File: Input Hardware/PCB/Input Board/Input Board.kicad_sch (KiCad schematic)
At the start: 6 parts

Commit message: end me
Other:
- sheet Demux & Amplifier 1 renamed Mux & Amplifier 3
- sheet Demux & Amplifier 2 renamed Mux & Amplifier 2
- sheet Demux & Amplifier 3 renamed Mux & Amplifier 4
- sheet Demux & Amplifier 4 renamed Mux & Amplifier 1
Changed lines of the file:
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@@
 			(color 0 0 0 0.0000)
 		)
-		(property "Sheetname" "Demux & Amplifier 4"
+		(property "Sheetname" "Mux & Amplifier 1"
 			(at 50.8 25.9584 0)
 			(effects
@@
 	)
 	(sheet
-		(at 135.89 153.67)
-		(size 27.94 24.13)
+		(at 139.7 139.7)
+		(size 25.4 25.4)
 		(exclude_from_sim no)
 		(in_bom yes)
@@
 		)
 		(property "Sheetname" "Power"
-			(at 135.89 152.9584 0)
+			(at 139.7 138.9884 0)
 			(effects
 				(font
@@
 		)
 		(property "Sheetfile" "power.kicad_sch"
-			(at 135.89 178.3846 0)
+			(at 139.7 165.6846 0)
 			(effects
 				(font
@@
 			(color 0 0 0 0.0000)
 		)
-		(property "Sheetname" "Demux & Amplifier 3"
+		(property "Sheetname" "Mux & Amplifier 4"
 			(at 50.8 102.1584 0)
 			(effects
@@
 			(color 0 0 0 0.0000)
 		)
-		(property "Sheetname" "Demux & Amplifier 1"
+		(property "Sheetname" "Mux & Amplifier 3"
 			(at 50.8 76.7584 0)
 			(effects
@@
 			(color 0 0 0 0.0000)
 		)
-		(property "Sheetname" "Demux & Amplifier 2"
+		(property "Sheetname" "Mux & Amplifier 2"
 			(at 50.8 51.3584 0)
 			(effects

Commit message: GM
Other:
- added sheet OLED (display.kicad_sch)
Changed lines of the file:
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@@
+	)
+	(sheet
+		(at 190.5 63.5)
+		(size 12.7 25.4)
+		(exclude_from_sim no)
+		(in_bom yes)
+		(on_board yes)
+		(dnp no)
+		(fields_autoplaced yes)
+		(stroke
+			(width 0.1524)
+			(type solid)
+		)
+		(fill
+			(color 0 0 0 0.0000)
+		)
+		(property "Sheetname" "OLED"
+			(at 190.5 62.7884 0)
+			(effects
+				(font
+					(size 1.27 1.27)
+				)
+				(justify left bottom)
+			)
+		)
+		(property "Sheetfile" "display.kicad_sch"
+			(at 190.5 89.4846 0)
+			(effects
+				(font
+					(size 1.27 1.27)
+				)
+				(justify left top)
+			)
+		)
+		(instances
+			(project "Input Board"
+				(path "/198ad8d1-66e3-4deb-889c-1af2b81e67c3"
+					(page "15")
+				)
+			)
+		)
 	)
 	(sheet

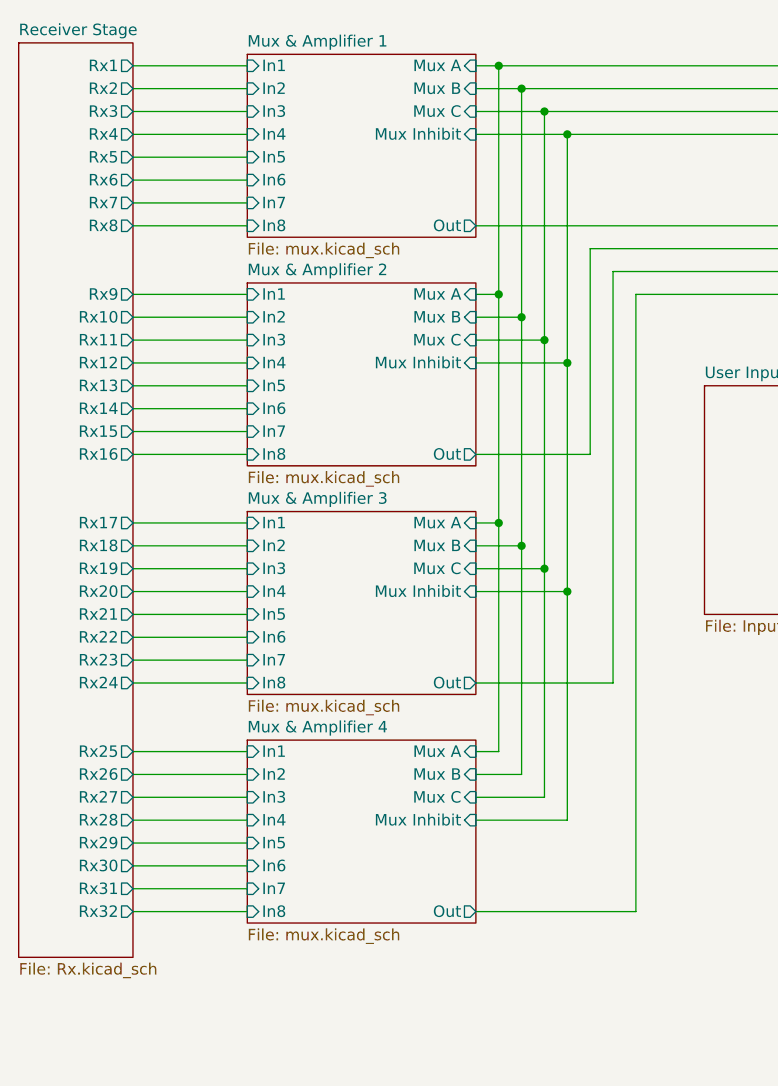
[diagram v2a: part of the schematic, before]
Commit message: adc bandpass amp and rootpage update
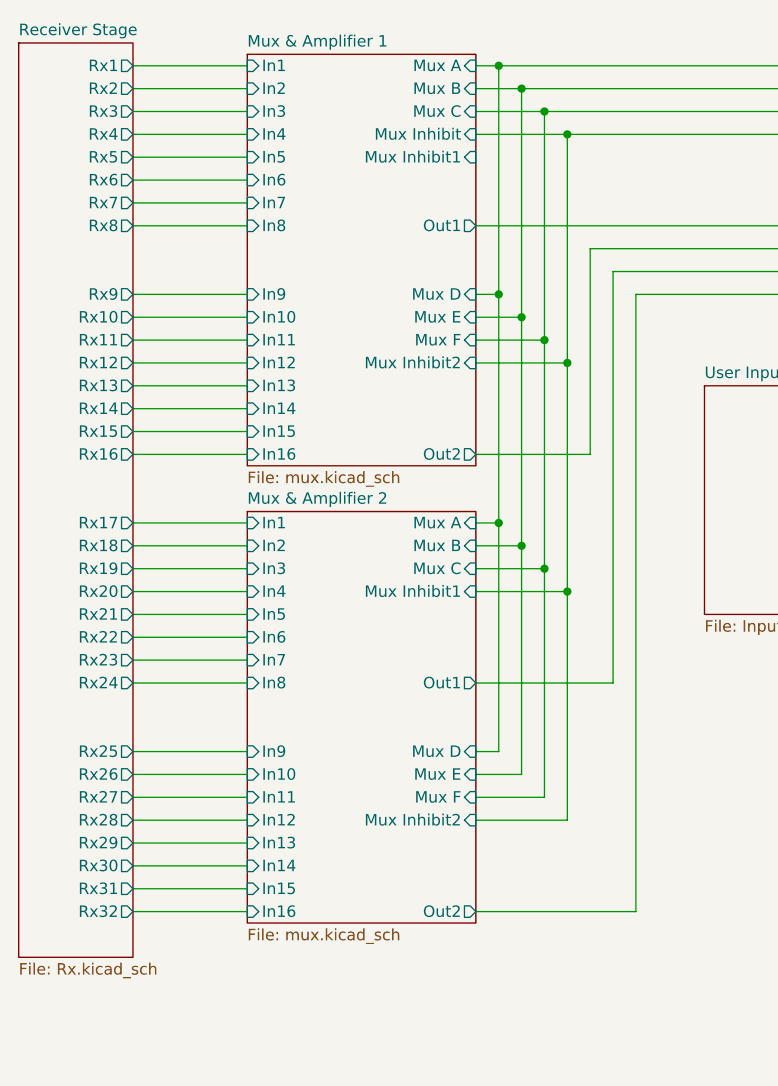
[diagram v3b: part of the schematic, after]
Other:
- removed sheet Mux & Amplifier 3
- removed sheet Mux & Amplifier 4
- sheet Mux & Amplifier 1 ports: added In10, In11, In12, In13, In14, In15, In16, In9, Mux D, Mux E, Mux F, Mux Inhibit1, Mux Inhibit2, Out1, Out2; removed Out
- sheet Mux & Amplifier 2 ports: added In10, In11, In12, In13, In14, In15, In16, In9, Mux D, Mux E, Mux F, Mux Inhibit1, Mux Inhibit2, Out1, Out2; removed Mux Inhibit, Out

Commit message: help
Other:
- sheet Mux & Amplifier 1 ports: added none; removed Mux Inhibit1, Mux Inhibit2
- sheet Mux & Amplifier 2 ports: added Mux Inhibit; removed Mux Inhibit1, Mux Inhibit2
- sheet User Input ports: added I_COM, O_CENTER, O_COM, O_DOWN, O_LEFT, O_RIGHT, O_UP, S_A, S_B, S_PUSH; removed none
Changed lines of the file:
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@@
 	)
 	(junction
-		(at 86.36 60.96)
+		(at 88.9 71.12)
 		(diameter 0)
 		(color 0 0 0 0)
@@
 	)
 	(junction
-		(at 86.36 86.36)
-		(diameter 0)
-		(color 0 0 0 0)
-	)
-	(junction
 		(at 78.74 78.74)
 		(diameter 0)
@@
 		(color 0 0 0 0)
 	)
-	(junction
-		(at 86.36 35.56)
-		(diameter 0)
-		(color 0 0 0 0)
-	)
 	(wire
 		(pts
@@
 	(wire
 		(pts
-			(xy 76.2 86.36) (xy 86.36 86.36)
-		)
-		(stroke
-			(width 0)
-			(type default)
-		)
-	)
-	(wire
-		(pts
 			(xy 81.28 81.28) (xy 81.28 55.88)
 		)
@@
 	(wire
 		(pts
-			(xy 86.36 35.56) (xy 139.7 35.56)
-		)
-		(stroke
-			(width 0)
-			(type default)
-		)
-	)
-	(wire
-		(pts
 			(xy 78.74 27.94) (xy 139.7 27.94)
 		)
@@
 	(wire
 		(pts
-			(xy 86.36 86.36) (xy 86.36 60.96)
-		)
-		(stroke
-			(width 0)
-			(type default)
-		)
-	)
-	(wire
-		(pts
 			(xy 83.82 33.02) (xy 139.7 33.02)
 		)
@@
 	(wire
 		(pts
-			(xy 76.2 35.56) (xy 86.36 35.56)
+			(xy 76.2 35.56) (xy 139.7 35.56)
 		)
 		(stroke
@@
 	(wire
 		(pts
-			(xy 76.2 111.76) (xy 86.36 111.76)
-		)
-		(stroke
-			(width 0)
-			(type default)
-		)
-	)
-	(wire
-		(pts
 			(xy 38.1 27.94) (xy 50.8 27.94)
 		)
@@
 	(wire
 		(pts
+			(xy 88.9 86.36) (xy 88.9 71.12)
+		)
+		(stroke
+			(width 0)
+			(type default)
+		)
+	)
+	(wire
+		(pts
 			(xy 38.1 96.52) (xy 50.8 96.52)
 		)
@@
 	(wire
 		(pts
-			(xy 86.36 111.76) (xy 86.36 86.36)
-		)
-		(stroke
-			(width 0)
-			(type default)
-		)
-	)
-	(wire
-		(pts
 			(xy 38.1 121.92) (xy 50.8 121.92)
 		)
@@
 	(wire
 		(pts
-			(xy 86.36 60.96) (xy 86.36 35.56)
-		)
-		(stroke
-			(width 0)
-			(type default)
-		)
-	)
-	(wire
-		(pts
 			(xy 38.1 30.48) (xy 50.8 30.48)
 		)
@@
 	(wire
 		(pts
+			(xy 76.2 86.36) (xy 88.9 86.36)
+		)
+		(stroke
+			(width 0)
+			(type default)
+		)
+	)
+	(wire
+		(pts
 			(xy 76.2 55.88) (xy 81.28 55.88)
 		)
@@
 		(pts
 			(xy 38.1 55.88) (xy 50.8 55.88)
-		)
-		(stroke
-			(width 0)
-			(type default)
-		)
-	)
-	(wire
-		(pts
-			(xy 76.2 60.96) (xy 86.36 60.96)
 		)
 		(stroke
@@
 	(sheet
 		(at 101.6 63.5)
-		(size 25.4 25.4)
+		(size 25.4 38.1)
 		(exclude_from_sim no)
 		(in_bom yes)
@@
 		)
 		(property "Sheetfile" "Input.kicad_sch"
-			(at 101.6 89.4846 0)
+			(at 101.6 102.1846 0)
 			(effects
 				(font
@@
 				)
 				(justify left top)
+			)
+		)
+		(pin "I_COM" input
+			(at 127 66.04 0)
+			(effects
+				(font
+					(size 1.27 1.27)
+				)
+				(justify right)
+			)
+		)
+		(pin "O_CENTER" output
+			(at 127 78.74 0)
+			(effects
+				(font
+					(size 1.27 1.27)
+				)
+				(justify right)
+			)
+		)
+		(pin "O_COM" input
+			(at 127 68.58 0)
+			(effects
+				(font
+					(size 1.27 1.27)
+				)
+				(justify right)
+			)
+		)
+		(pin "O_DOWN" output
+			(at 127 83.82 0)
+			(effects
+				(font
+					(size 1.27 1.27)
+				)
+				(justify right)
+			)
+		)
+		(pin "O_LEFT" output
+			(at 127 73.66 0)
+			(effects
+				(font
+					(size 1.27 1.27)
+				)
+				(justify right)
+			)
+		)
+		(pin "O_RIGHT" output
+			(at 127 76.2 0)
+			(effects
+				(font
+					(size 1.27 1.27)
+				)
+				(justify right)
+			)
+		)
+		(pin "O_UP" output
+			(at 127 81.28 0)
+			(effects
+				(font
+					(size 1.27 1.27)
+				)
+				(justify right)
+			)
+		)
+		(pin "S_A" output
+			(at 127 88.9 0)
+			(effects
+				(font
+					(size 1.27 1.27)
+				)
+				(justify right)
+			)
+		)
+		(pin "S_B" output
+			(at 127 91.44 0)
+			(effects
+				(font
+					(size 1.27 1.27)
+				)
+				(justify right)
+			)
+		)
+		(pin "S_PUSH" output
+			(at 127 93.98 0)
+			(effects
+				(font
+					(size 1.27 1.27)
+				)
+				(justify right)
 			)
 		)
@@
 			)
 		)
-		(pin "Mux Inhibit1" input
-			(at 76.2 86.36 0)
-			(effects
-				(font
-					(size 1.27 1.27)
-				)
-				(justify right)
-			)
-		)
 		(pin "Out1" output
 			(at 76.2 96.52 0)
@@
 			)
 		)
-		(pin "Mux Inhibit2" input
-			(at 76.2 111.76 0)
-			(effects
-				(font
-					(size 1.27 1.27)
-				)
-				(justify right)
-			)
-		)
 		(pin "Mux F" input
 			(at 76.2 109.22 0)
@@
 		(pin "Mux E" input
 			(at 76.2 106.68 0)
+			(effects
+				(font
+					(size 1.27 1.27)
+				)
+				(justify right)
+			)
+		)
+		(pin "Mux Inhibit" input
+			(at 76.2 86.36 0)
 			(effects
 				(font
@@
 			)
 		)
-		(pin "Mux Inhibit1" input
-			(at 76.2 38.1 0)
-			(effects
-				(font
-					(size 1.27 1.27)
-				)
-				(justify right)
-			)
-		)
 		(pin "Out2" output
 			(at 76.2 71.12 0)
 			(effects
 				(font
-					(size 1.27 1.27)
-				)
-				(justify right)
-			)
-		)
-		(pin "Mux Inhibit2" input
-			(at 76.2 60.96 0)
-			(effects
-				(font

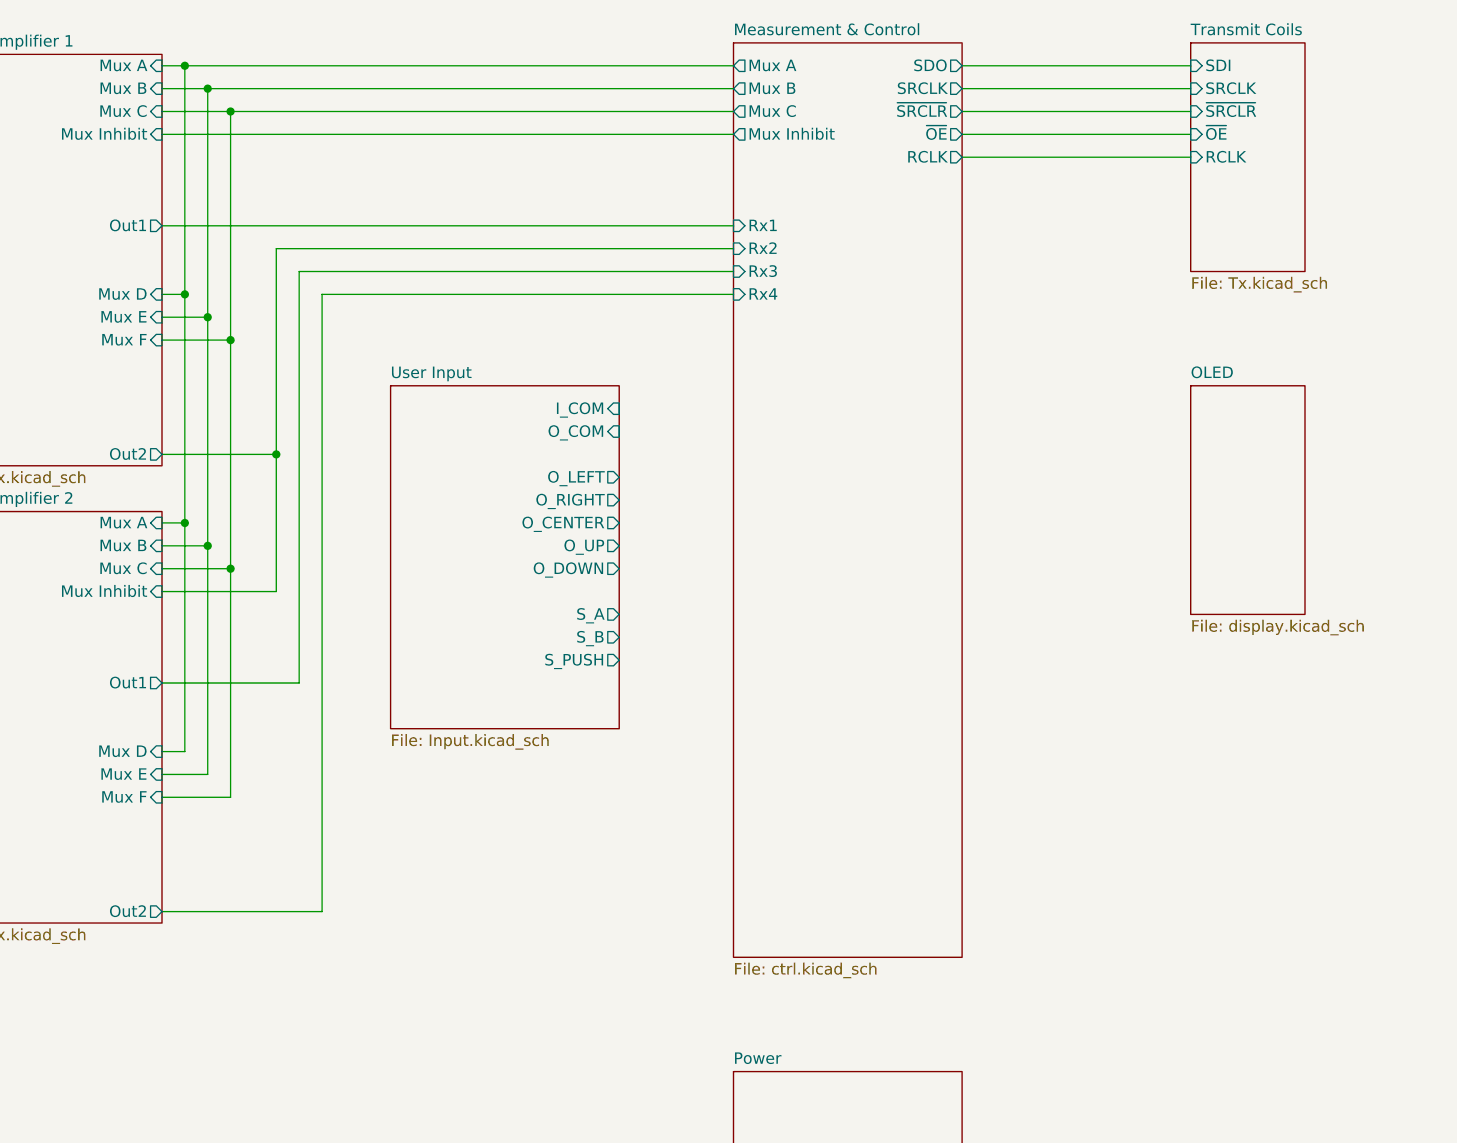
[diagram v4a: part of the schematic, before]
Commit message: Revert "images and pcb stuff"
This reverts commit 6978c7447e140ee759e19aaebffdac22097ec1b9.
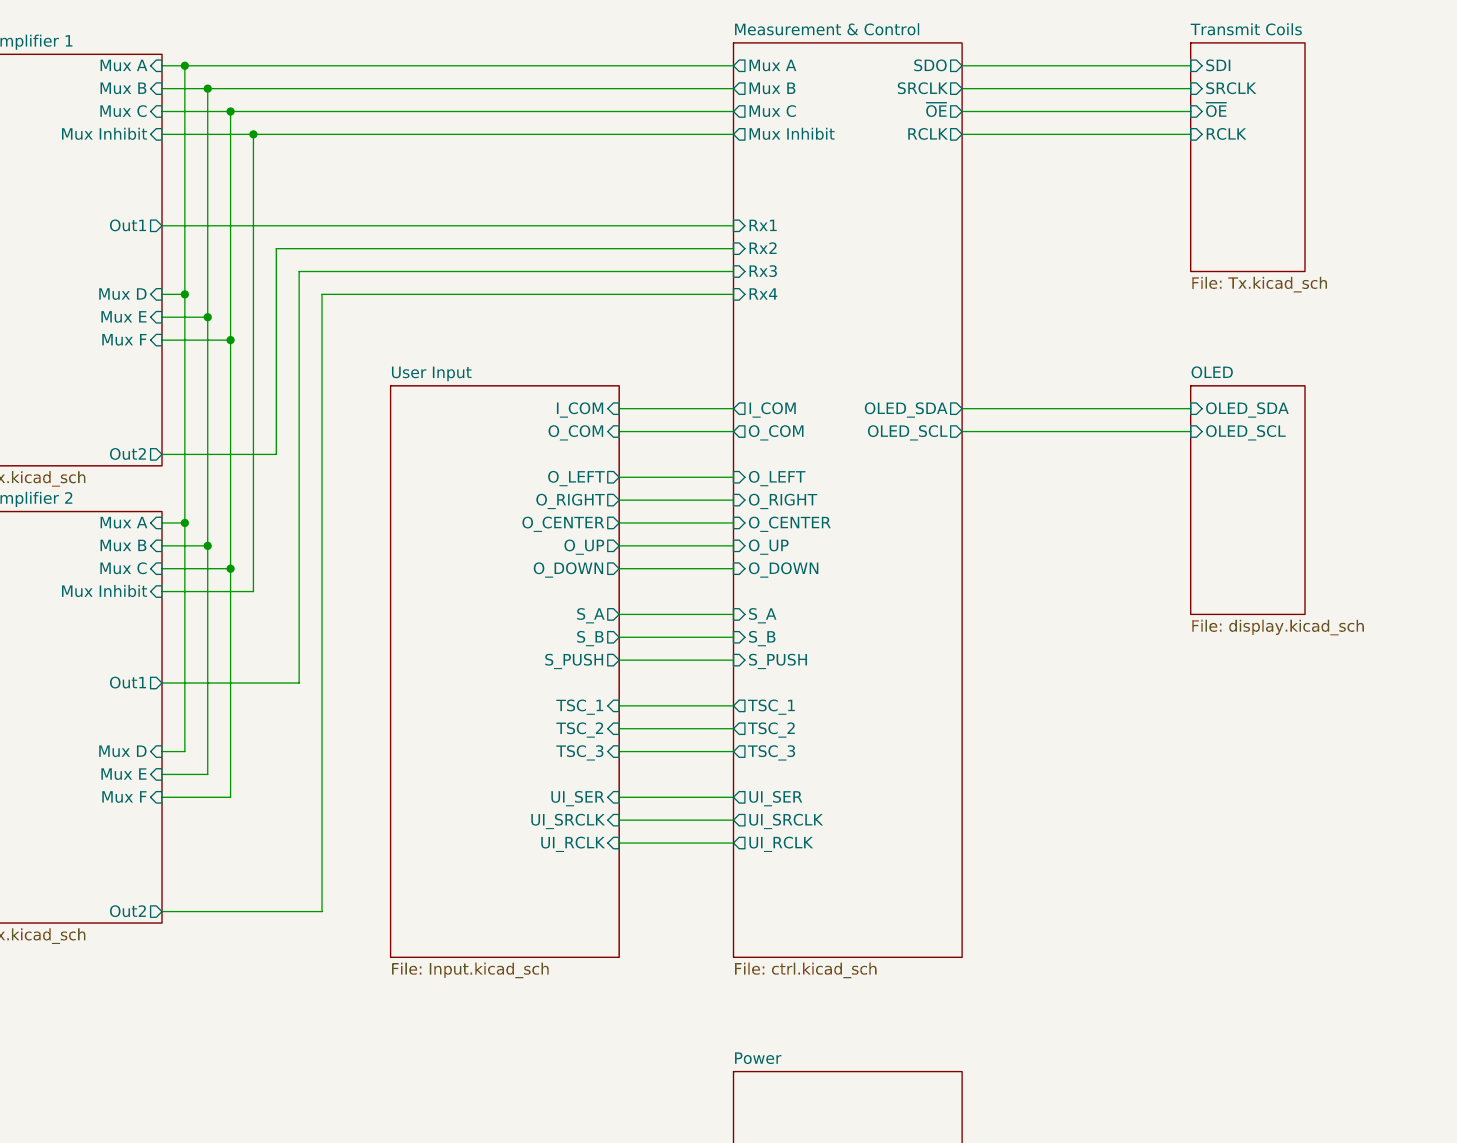
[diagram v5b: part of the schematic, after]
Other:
- sheet Measurement & Control ports: added I_COM, OLED_SCL, OLED_SDA, O_CENTER, O_COM, O_DOWN, O_LEFT, O_RIGHT, O_UP, S_A, S_B, S_PUSH, TSC_1, TSC_2, TSC_3, UI_RCLK, UI_SER, UI_SRCLK; removed ~{SRCLR}
- sheet OLED ports: added OLED_SCL, OLED_SDA; removed none
- sheet Transmit Coils ports: added none; removed ~{SRCLR}
- sheet User Input ports: added TSC_1, TSC_2, TSC_3, UI_RCLK, UI_SER, UI_SRCLK; removed none

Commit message: stmcube model and fixes
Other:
- note added: "Broken Stuff/Fixes/Recs: > Input Offset Wiring > Rotary Encoder Wiring > No names on buttons if possible to allow for maximum flexibility (potentially ontop instead?) > OSC_OUT conflict with Cube"
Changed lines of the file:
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@@
 	(generator_version "9.0")
 	(paper "A4")
+	(rectangle
+		(start 186.69 109.22)
+		(end 246.38 153.67)
+		(stroke
+			(width 0)
+			(type default)
+		)
+		(fill
+			(type none)
+		)
+	)
+	(text "Broken Stuff/Fixes/Recs:\n\n> Input Offset Wiring\n> Rotary Encoder Wiring\n> No names on buttons if possible to allow for maximum \nflexibility (potentially ontop instead?)\n> OSC_OUT conflict with Cube"
+		(exclude_from_sim no)
+		(at 187.96 118.11 0)
+		(effects
+			(font
+				(size 1.27 1.27)
+			)
+			(justify left)
+		)
+	)
 	(junction
 		(at 83.82 58.42)

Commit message: Fix files idc
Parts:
- renumbered H1 to H101, H2 to H102, H3 to H103, H4 to H104, H5 to H105, H6 to H106
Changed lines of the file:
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@@
 		(dnp no)
 		(fields_autoplaced yes)
-		(property "Reference" "H4"
+		(property "Reference" "H104"
 			(at 49.53 180.3399 0)
 			(effects
@@
 			(project "Input Board"
 				(path "/198ad8d1-66e3-4deb-889c-1af2b81e67c3"
-					(reference "H4")
+					(reference "H104")
 					(unit 1)
 				)
@@
 		(dnp no)
 		(fields_autoplaced yes)
-		(property "Reference" "H1"
+		(property "Reference" "H101"
 			(at 49.53 165.0999 0)
 			(effects
@@
 			(project ""
 				(path "/198ad8d1-66e3-4deb-889c-1af2b81e67c3"
-					(reference "H1")
+					(reference "H101")
 					(unit 1)
 				)
@@
 		(dnp no)
 		(fields_autoplaced yes)
-		(property "Reference" "H3"
+		(property "Reference" "H103"
 			(at 49.53 175.2599 0)
 			(effects
@@
 			(project "Input Board"
 				(path "/198ad8d1-66e3-4deb-889c-1af2b81e67c3"
-					(reference "H3")
+					(reference "H103")
 					(unit 1)
 				)
@@
 		(dnp no)
 		(fields_autoplaced yes)
-		(property "Reference" "H2"
+		(property "Reference" "H102"
 			(at 49.53 170.1799 0)
 			(effects
@@
 			(project "Input Board"
 				(path "/198ad8d1-66e3-4deb-889c-1af2b81e67c3"
-					(reference "H2")
+					(reference "H102")
 					(unit 1)
 				)
@@
 		(dnp no)
 		(fields_autoplaced yes)
-		(property "Reference" "H5"
+		(property "Reference" "H105"
 			(at 49.53 185.4199 0)
 			(effects
@@
 			(project "Input Board"
 				(path "/198ad8d1-66e3-4deb-889c-1af2b81e67c3"
-					(reference "H5")
+					(reference "H105")
 					(unit 1)
 				)
@@
 		(dnp no)
 		(fields_autoplaced yes)
-		(property "Reference" "H6"
+		(property "Reference" "H106"
 			(at 49.53 190.4999 0)
 			(effects
@@
 			(project "Input Board"
 				(path "/198ad8d1-66e3-4deb-889c-1af2b81e67c3"
-					(reference "H6")
+					(reference "H106")
 					(unit 1)
 				)
@@
 			(project "Input Board"
 				(path "/198ad8d1-66e3-4deb-889c-1af2b81e67c3"
-					(page "14")
+					(page "12")
 				)
 			)
@@
 			(project "Input Board"
 				(path "/198ad8d1-66e3-4deb-889c-1af2b81e67c3"
-					(page "11")
+					(page "9")
 				)
 			)
@@
 			(project "Input Board"
 				(path "/198ad8d1-66e3-4deb-889c-1af2b81e67c3"
-					(page "13")
+					(page "11")
 				)
 			)
@@
 			(project "Input Board"
 				(path "/198ad8d1-66e3-4deb-889c-1af2b81e67c3"
-					(page "4")
+					(page "8")
 				)
 			)
@@
 			(project "Input Board"
 				(path "/198ad8d1-66e3-4deb-889c-1af2b81e67c3"
-					(page "15")
+					(page "13")
 				)
 			)
@@
 			(project "Input Board"
 				(path "/198ad8d1-66e3-4deb-889c-1af2b81e67c3"
-					(page "12")
-				)
-			)
+					(page "10")
+				)
+			)

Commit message: Change topology
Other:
- sheet Mux & Amplifier 1 renamed Mux 1
- sheet Receiver Stage renamed Receiver Coils
- removed sheet Mux & Amplifier 2
- added sheet Amplifiers (amp.kicad_sch)
- added sheet Mux 2 (mux.kicad_sch)
- added sheet Mux 3 (mux.kicad_sch)
- added sheet Mux 4 (mux.kicad_sch)
- sheet Mux 1 ports: added none; removed In10, In11, In12, In13, In14, In15, In16, In9, Mux D, Mux E, Mux F, Out2
